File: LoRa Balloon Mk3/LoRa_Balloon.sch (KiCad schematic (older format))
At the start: 62 parts, among them J1 Qwicc_6-pin, J2 Qwiic_4pin, U1 SKY67013-396LF_CID141, U2 SX1272IMLTRICT-ND_CID104, U3 SKY67013-396LF_CID141, U4 XCL205, U5 PE4259_CID105, U6 ATMEGA328P-MMH, X1 X1E0000210162_CID142, X2 7A-12.000MAAJ-T_CID117

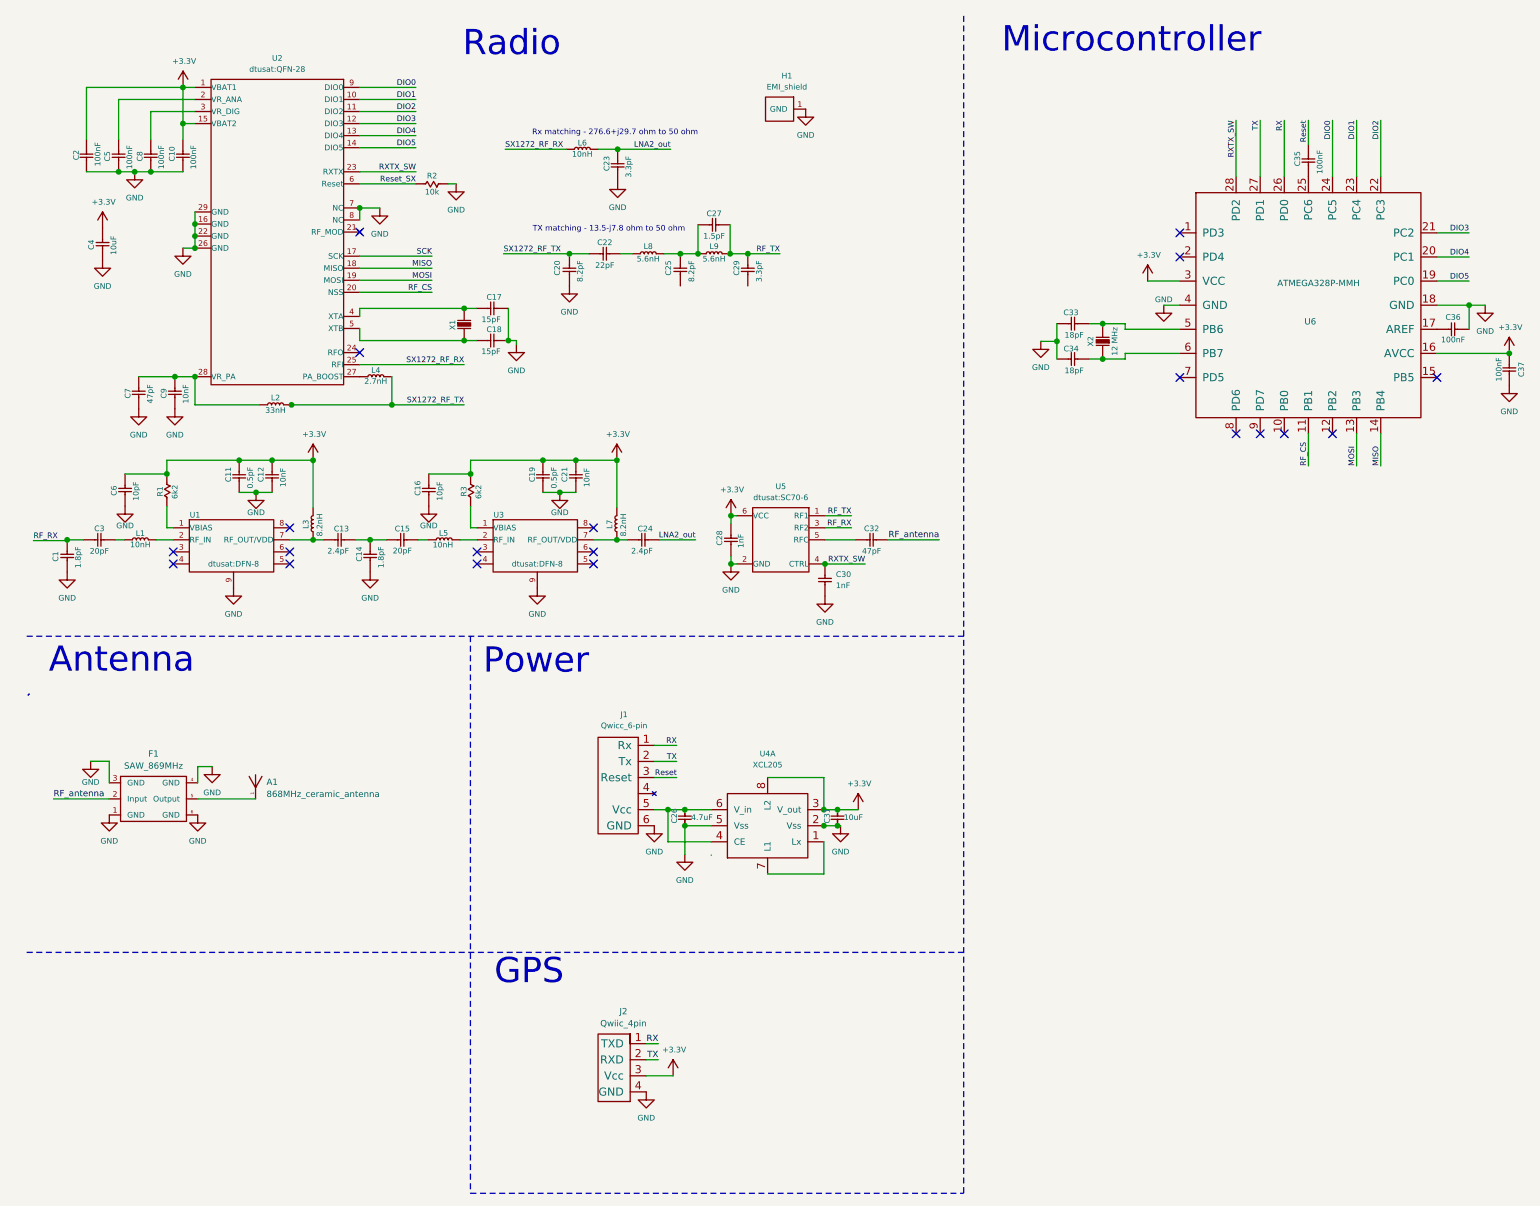
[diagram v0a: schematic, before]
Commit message: Created and added new component STEP files
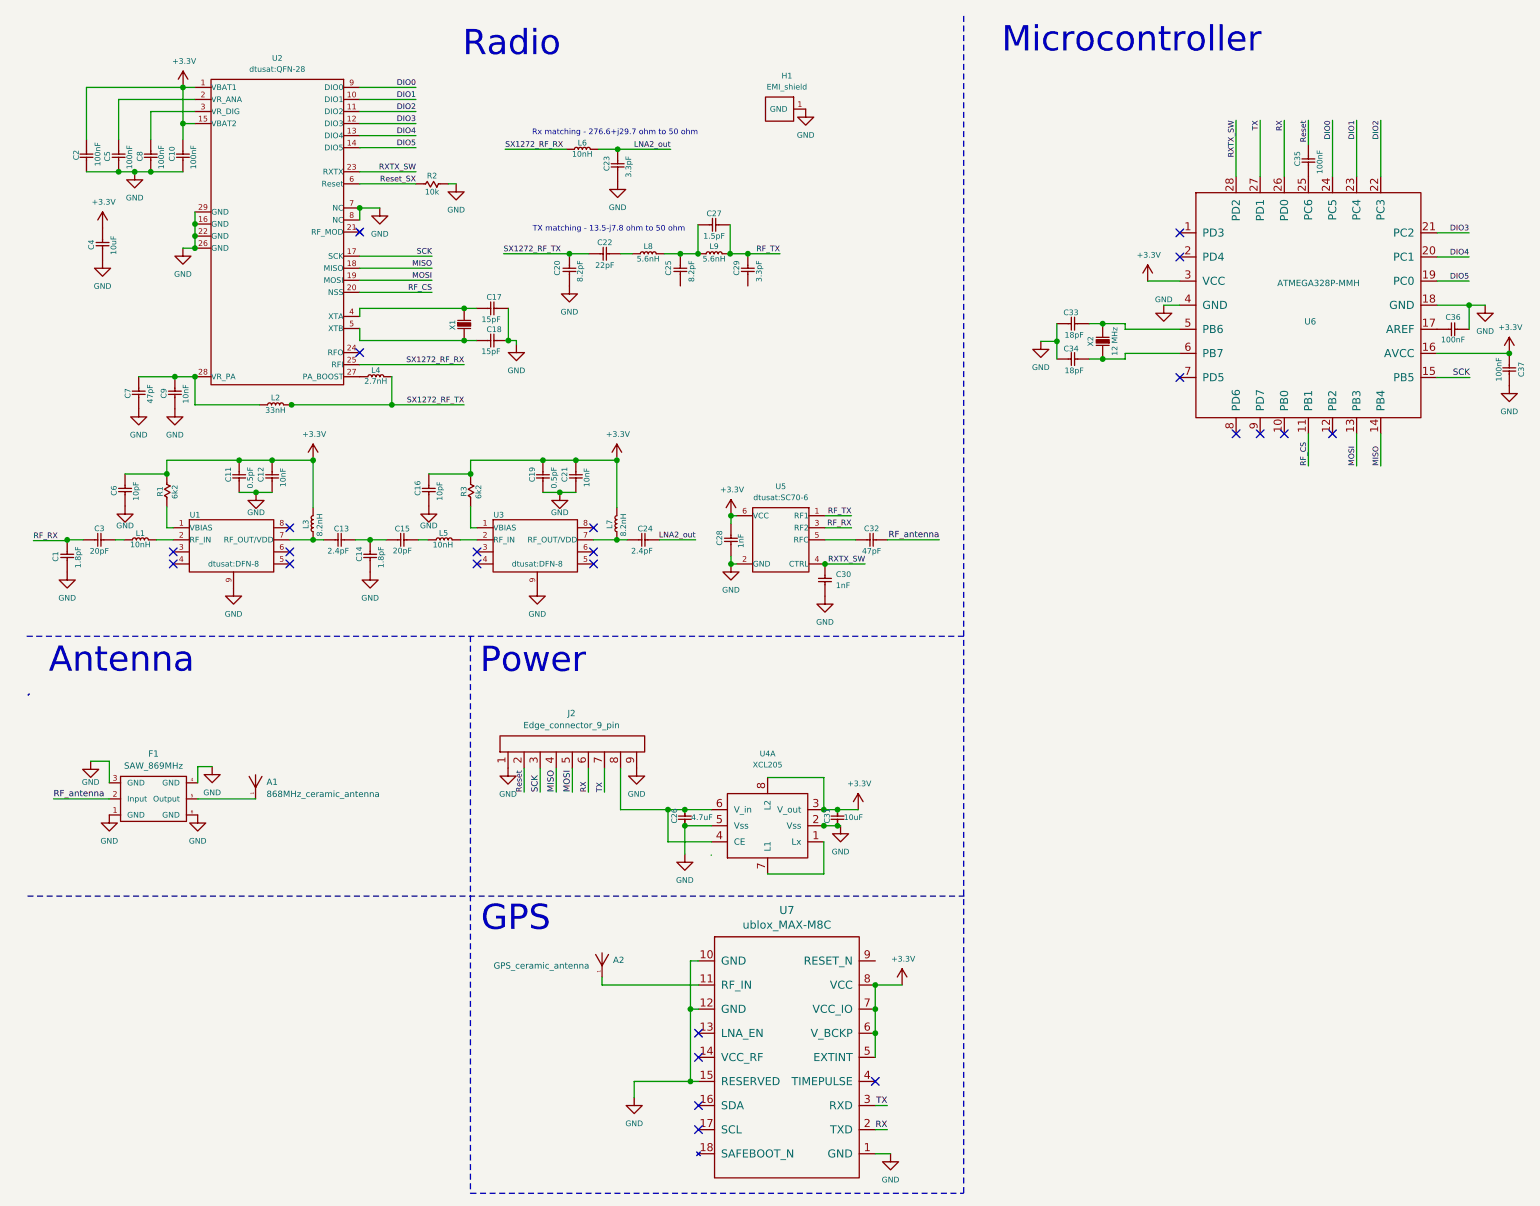
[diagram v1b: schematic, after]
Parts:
- removed J1: Qwicc_6-pin, dtusat:qwiic_6pin, symbol connectors:Qwicc_6-pin
- removed J2: Qwiic_4pin, dtusat:Qwiic_4-pin, symbol connectors:Qwiic_4pin
- added A2: GPS_ceramic_antenna, dtusat:Ceramic_Antenna, symbol dtusat-other:GPS_ceramic_antenna
- added J2: Edge_connector_9_pin, dtusat:Edge_connector_9_pin, symbol dtusat-other:Edge_connector_9_pin
- added U7: ublox_MAX-M8C, dtusat:ublox_MAX-M8C, symbol dtusat-ic:ublox_MAX-M8C
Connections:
- net +3V3: now also U7.5 (EXTINT), U7.6 (V_BCKP), U7.7 (VCC_IO), U7.8 (VCC)
- net GND: now also J2.1, J2.9, U7.1 (GND), U7.10 (GND), U7.12 (GND), U7.15 (RESERVED)
- net MISO: now also J2.4
- net MOSI: now also J2.5
- net RX: now also J2.6, U7.2 (TXD)
- net Reset: now also J2.2
- net SCK: now also U6.15 (PB5), J2.3
- net TX: now also J2.7, U7.3 (RXD)
- net at C26.1, U4.4 (CE), U4.6 (V_in): now also J2.8
- new net: A2.1, U7.11 (RF_IN)
- no-connect marks 20 -> 24
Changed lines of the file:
@@
 Wire Wire Line
 	6880 2495 6880 2385
-$Comp
-L connectors:Qwicc_6-pin J1
-U 1 1 5DFE3169
-P 4175 5259
-F 0 "J1" V 3733 5271 35  0000 C CNN
-F 1 "Qwicc_6-pin" V 3802 5271 35  0000 C CNN
-F 2 "dtusat:qwiic_6pin" H 3925 5159 35  0001 C CNN
-F 3 "" H 3925 5159 35  0001 C CNN
-	1    4175 5259
-	0    1    1    0
-$EndComp
-$Comp
-L dtusat-power:GND #PWR028
-U 1 1 5DFEC0C6
-P 4375 5509
-F 0 "#PWR028" H 4375 5259 35  0001 C CNN
-F 1 "GND" H 4375 5347 35  0000 C CNN
-F 2 "" H 4375 5509 35  0000 C CNN
-F 3 "" H 4375 5509 35  0000 C CNN
-	1    4375 5509
-	1    0    0    -1
-$EndComp
-Text Label 4515 5009 2    35   ~ 0
+Text Label 3965 5300 1    35   ~ 0
 RX
-Text Label 4515 5109 2    35   ~ 0
+Text Label 4065 5300 1    35   ~ 0
 TX
-Wire Wire Line
-	4515 5009 4375 5009
-Wire Wire Line
-	4375 5109 4515 5109
 Text Label 8295 1120 3    35   ~ 0
 RX
@@
 Wire Wire Line
 	2118 2890 2742 2890
-Text Label 4515 5209 2    35   ~ 0
-Reset
-Wire Wire Line
-	4375 5209 4515 5209
 Wire Wire Line
 	1517 990  1042 990
@@
 	2542 1440 2892 1440
 Wire Wire Line
-	4375 5409 4460 5409
-Wire Wire Line
 	4730 5609 4460 5609
-Wire Wire Line
-	4460 5609 4460 5409
-Connection ~ 4460 5409
 Wire Wire Line
 	4460 5409 4565 5409
@@
 	470  4330 6300 4330
 Wire Notes Line
-	470  6297 6300 6297
+	475  5947 6305 5947
 Text Notes 1513 4573 2    157  ~ 0
 Antenna
-Text Notes 3969 4579 2    157  ~ 0
+Text Notes 3950 4575 2    157  ~ 0
 Power\n
 Text Notes 8153 714  2    157  ~ 0
@@
 	5515 5509 5534 5509
 Connection ~ 5515 5509
-$Comp
-L connectors:Qwiic_4pin J2
-U 1 1 5DFAC587
-P 4185 7005
-F 0 "J2" H 4183 7346 39  0000 C CNN
-F 1 "Qwiic_4pin" H 4183 7271 39  0000 C CNN
-F 2 "dtusat:Qwiic_4-pin" H 4185 6945 39  0001 C CNN
-F 3 "" H 4185 6945 39  0001 C CNN
-	1    4185 7005
-	1    0    0    -1
-$EndComp
-Wire Wire Line
-	4325 6865 4400 6865
-Wire Wire Line
-	4325 6965 4400 6965
+Wire Wire Line
+	5750 7400 5825 7400
+Wire Wire Line
+	5750 7250 5825 7250
 $Comp
 L dtusat-power:GND #PWR027
 U 1 1 5DFC38A0
-P 4325 7165
-F 0 "#PWR027" H 4325 6915 35  0001 C CNN
-F 1 "GND" H 4325 7003 35  0000 C CNN
-F 2 "" H 4325 7165 35  0000 C CNN
-F 3 "" H 4325 7165 35  0000 C CNN
-	1    4325 7165
+P 5845 7550
+F 0 "#PWR027" H 5845 7300 35  0001 C CNN
+F 1 "GND" H 5845 7388 35  0000 C CNN
+F 2 "" H 5845 7550 35  0000 C CNN
+F 3 "" H 5845 7550 35  0000 C CNN
+	1    5845 7550
 	1    0    0    -1
 $EndComp
@@
 L dtusat-power:+3.3V #PWR029
 U 1 1 5DFC4AFB
-P 4492 7065
-F 0 "#PWR029" H 4492 6915 35  0001 C CNN
-F 1 "+3.3V" H 4499 7227 35  0000 C CNN
-F 2 "" H 4492 7065 35  0000 C CNN
-F 3 "" H 4492 7065 35  0000 C CNN
-	1    4492 7065
-	1    0    0    -1
-$EndComp
-Wire Wire Line
-	4325 7065 4492 7065
+P 5917 6500
+F 0 "#PWR029" H 5917 6350 35  0001 C CNN
+F 1 "+3.3V" H 5924 6662 35  0000 C CNN
+F 2 "" H 5917 6500 35  0000 C CNN
+F 3 "" H 5917 6500 35  0000 C CNN
+	1    5917 6500
+	1    0    0    -1
+$EndComp
+Wire Wire Line
+	5750 6500 5917 6500
 Wire Notes Line
 	3231 7796 6300 7796
@@
 Wire Notes Line
 	3231 4329 3231 7796
-Text Notes 3813 6511 2    157  ~ 0
+Text Notes 3730 6180 2    157  ~ 0
 GPS\n
 Wire Wire Line
@@
 	7995 1120 7995 1470
 Connection ~ 9695 2570
-NoConn ~ 9245 2720
 NoConn ~ 8595 3070
 NoConn ~ 8295 3070
@@
 NoConn ~ 7645 1820
 NoConn ~ 7645 1970
-Text Label 4400 6965 2    39   ~ 0
+Text Label 5825 7250 2    39   ~ 0
 TX
-Text Label 4400 6865 2    39   ~ 0
+Text Label 5825 7400 2    39   ~ 0
 RX
+$Comp
+L dtusat-ic:ublox_MAX-M8C U7
+U 1 1 630D6E38
+P 5200 6950
+F 0 "U7" H 5200 7865 50  0000 C CNN
+F 1 "ublox_MAX-M8C" H 5200 7774 50  0000 C CNN
+F 2 "dtusat:ublox_MAX-M8C" H 5200 6950 50  0001 C CNN
+F 3 "" H 5200 6950 50  0001 C CNN
+	1    5200 6950
+	1    0    0    -1
+$EndComp
+Wire Wire Line
+	5750 7550 5845 7550
+$Comp
+L dtusat-power:GND #PWR0101
+U 1 1 631145D8
+P 4250 7200
+F 0 "#PWR0101" H 4250 6950 35  0001 C CNN
+F 1 "GND" H 4250 7038 35  0000 C CNN
+F 2 "" H 4250 7200 35  0000 C CNN
+F 3 "" H 4250 7200 35  0000 C CNN
+	1    4250 7200
+	1    0    0    -1
+$EndComp
+$Comp
+L dtusat-other:GPS_ceramic_antenna A2
+U 1 1 63129460
+P 4050 6380
+F 0 "A2" H 4118 6415 39  0000 L CNN
+F 1 "GPS_ceramic_antenna" H 3375 6380 39  0000 L CNN
+F 2 "dtusat:Ceramic_Antenna" H 4050 6380 39  0001 C CNN
+F 3 "" H 4050 6380 39  0001 C CNN
+	1    4050 6380
+	1    0    0    -1
+$EndComp
+Wire Wire Line
+	4050 6450 4050 6500
+Wire Wire Line
+	4050 6500 4650 6500
+Wire Wire Line
+	4250 7200 4250 7100
+Wire Wire Line
+	4250 7100 4600 7100
+Wire Wire Line
+	4650 6350 4600 6350
+Wire Wire Line
+	4600 6350 4600 6650
+Wire Wire Line
+	4600 6650 4650 6650
+Wire Wire Line
+	4600 6650 4600 7100
+Connection ~ 4600 6650
+Connection ~ 4600 7100
+Wire Wire Line
+	4600 7100 4650 7100
+Wire Wire Line
+	5750 6950 5750 6800
+Wire Wire Line
+	5750 6800 5750 6650
+Connection ~ 5750 6800
+Wire Wire Line
+	5750 6650 5750 6500
+Connection ~ 5750 6650
+Connection ~ 5750 6500
+NoConn ~ 4650 7400
+NoConn ~ 4650 7250
+NoConn ~ 4650 6950
+NoConn ~ 4650 6800
+NoConn ~ 5750 7100
+$Comp
+L dtusat-other:Edge_connector_9_pin J2
+U 1 1 631B851F
+P 3865 5050
+F 0 "J2" H 3860 5291 39  0000 C CNN
+F 1 "Edge_connector_9_pin" H 3860 5216 39  0000 C CNN
+F 2 "dtusat:Edge_connector_9_pin" H 3865 4500 39  0001 C CNN
+F 3 "" H 3865 4500 39  0001 C CNN
+	1    3865 5050
+	1    0    0    -1
+$EndComp
+$Comp
+L dtusat-power:GND #PWR0102
+U 1 1 631BAF34
+P 4265 5150
+F 0 "#PWR0102" H 4265 4900 35  0001 C CNN
+F 1 "GND" H 4265 4988 35  0000 C CNN
+F 2 "" H 4265 5150 35  0000 C CNN
+F 3 "" H 4265 5150 35  0000 C CNN
+	1    4265 5150
+	1    0    0    -1
+$EndComp
+$Comp
+L dtusat-power:GND #PWR0103
+U 1 1 631BBA18
+P 3465 5150
+F 0 "#PWR0103" H 3465 4900 35  0001 C CNN
+F 1 "GND" H 3465 4988 35  0000 C CNN
+F 2 "" H 3465 5150 35  0000 C CNN
+F 3 "" H 3465 5150 35  0000 C CNN
+	1    3465 5150
+	1    0    0    -1
+$EndComp
+Wire Wire Line
+	4460 5409 4460 5609
+Connection ~ 4460 5409
+Wire Wire Line
+	4165 5409 4165 5150
+Wire Wire Line
+	4165 5409 4460 5409
+Text Label 3865 5300 1    39   ~ 0
+MOSI
+Text Label 3765 5300 1    39   ~ 0
+MISO
+Text Label 3665 5300 1    39   ~ 0
+SCK
+Wire Wire Line
+	3665 5300 3665 5150
+Wire Wire Line
+	3765 5150 3765 5300
+Wire Wire Line
+	3865 5300 3865 5150
+Text Label 3565 5300 1    35   ~ 0
+Reset
+Wire Wire Line
+	3965 5300 3965 5150
+Wire Wire Line
+	4065 5150 4065 5300
+Wire Wire Line
+	3565 5300 3565 5150
+Text Label 9450 2720 2    39   ~ 0
+SCK
+Wire Wire Line
+	9245 2720 9450 2720
 $EndSCHEMATC

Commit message: Finished board layout
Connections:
- net RX: no longer U7.2 (TXD)
- net RXTX_SW: now also U6.7 (PD5); no longer U6.28 (PD2)
- net TX: no longer U7.3 (RXD)
- net GPS_RX: now reaches U6.1 (PD3)
- net GPS_RX: now also U7.3 (RXD)
- net GPS_TX: now reaches U6.2 (PD4)
- net GPS_TX: now also U7.2 (TXD)
- no-connect marks 24 -> 22
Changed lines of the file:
@@
 L dtusat-power:+3.3V #PWR038
 U 1 1 5E0270B1
-P 7445 2120
-F 0 "#PWR038" H 7445 1970 35  0001 C CNN
-F 1 "+3.3V" H 7452 2282 35  0000 C CNN
-F 2 "" H 7445 2120 35  0000 C CNN
-F 3 "" H 7445 2120 35  0000 C CNN
-	1    7445 2120
+P 7200 2120
+F 0 "#PWR038" H 7200 1970 35  0001 C CNN
+F 1 "+3.3V" H 7207 2282 35  0000 C CNN
+F 2 "" H 7200 2120 35  0000 C CNN
+F 3 "" H 7200 2120 35  0000 C CNN
+	1    7200 2120
 	1    0    0    -1
 $EndComp
@@
 	1    0    0    -1
 $EndComp
-Text Label 7995 1120 3    35   ~ 0
+Text Label 7400 2720 0    35   ~ 0
 RXTX_SW
 $Comp
@@
 	5515 5509 5534 5509
 Connection ~ 5515 5509
-Wire Wire Line
-	5750 7400 5825 7400
-Wire Wire Line
-	5750 7250 5825 7250
 $Comp
 L dtusat-power:GND #PWR027
@@
 Wire Wire Line
 	8445 1270 8445 1120
-Wire Wire Line
-	7645 2120 7445 2120
 $Comp
 L dtusat-power:GND #PWR039
@@
 Wire Wire Line
 	8145 1470 8145 1120
-Wire Wire Line
-	7995 1120 7995 1470
 Connection ~ 9695 2570
 NoConn ~ 8595 3070
@@
 NoConn ~ 8145 3070
 NoConn ~ 7995 3070
-NoConn ~ 7645 2720
-NoConn ~ 7645 1820
-NoConn ~ 7645 1970
-Text Label 5825 7250 2    39   ~ 0
-TX
-Text Label 5825 7400 2    39   ~ 0
-RX
+Text Label 6000 7250 2    39   ~ 0
+GPS_RX
+Text Label 6000 7400 2    39   ~ 0
+GPS_TX
 $Comp
 L dtusat-ic:ublox_MAX-M8C U7
@@
 Wire Wire Line
 	9245 2720 9450 2720
+Wire Wire Line
+	5750 7250 6000 7250
+Wire Wire Line
+	5750 7400 6000 7400
+Text Label 7395 1820 0    39   ~ 0
+GPS_RX
+Text Label 7395 1970 0    39   ~ 0
+GPS_TX
+Wire Wire Line
+	7395 1820 7645 1820
+Wire Wire Line
+	7395 1970 7645 1970
+Wire Wire Line
+	7200 2120 7645 2120
+Wire Wire Line
+	7400 2720 7645 2720
+NoConn ~ 7995 1470
 $EndSCHEMATC
